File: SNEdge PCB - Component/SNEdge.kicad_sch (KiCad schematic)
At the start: 47 parts, among them J1 RGB_OUT, J2 (R-Y)O, J3 (B-Y)O, J4 YO, J5 G_IN, J6 B_IN, J7 R_IN, U2 TS5V330CPWR

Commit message: Cleaned up component side
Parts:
- removed R2: 1k, Resistor_SMD:R_0805_2012Metric_Pad1.20x1.40mm_HandSolder, symbol Device:R_US
- removed R3: 820R, Resistor_SMD:R_0805_2012Metric_Pad1.20x1.40mm_HandSolder, symbol Device:R_US
- removed R4: 220R, Resistor_SMD:R_0805_2012Metric_Pad1.20x1.40mm_HandSolder, symbol Device:R_US
- removed R5: 470R, Resistor_SMD:R_0805_2012Metric_Pad1.20x1.40mm_HandSolder, symbol Device:R_US
- removed R6: 680R, Resistor_SMD:R_0805_2012Metric_Pad1.20x1.40mm_HandSolder, symbol Device:R_US
- R1: value 1k -> 75
- R21: value 1k -> 10k
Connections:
- net GND: now also R1.1
- net at C2.1: now also J3.1 (In)
- net at J4.1 (In): now also C3.1
- net at J2.1 (In): now also C1.1, R1.2; no longer R1.1
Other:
- moved on the sheet: J2, J3, J4

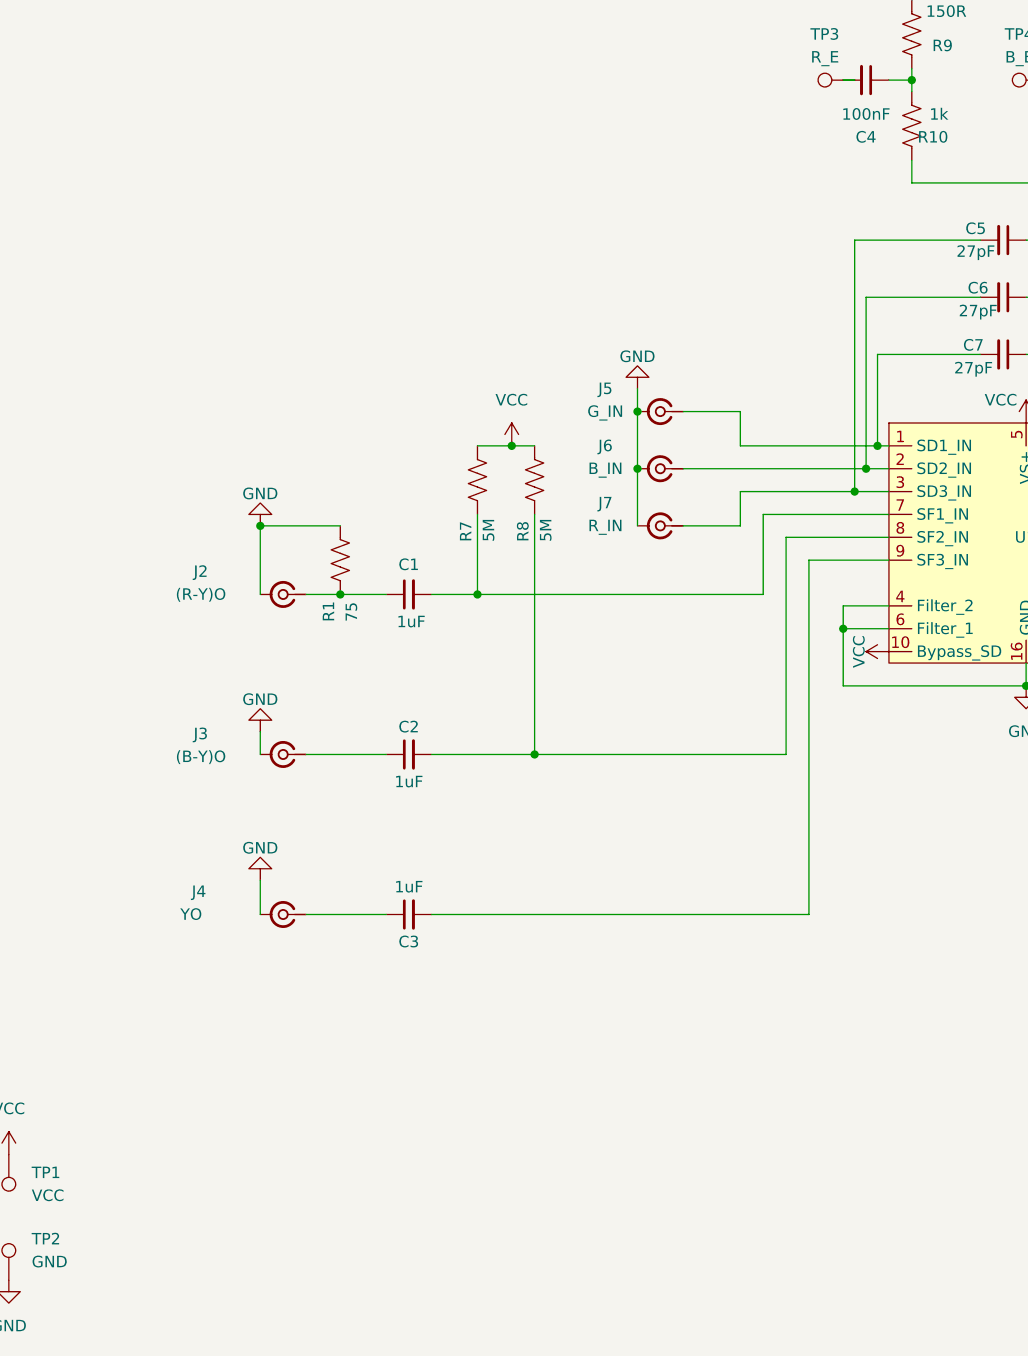
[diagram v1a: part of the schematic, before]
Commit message: Added voltage dividers on RGB input
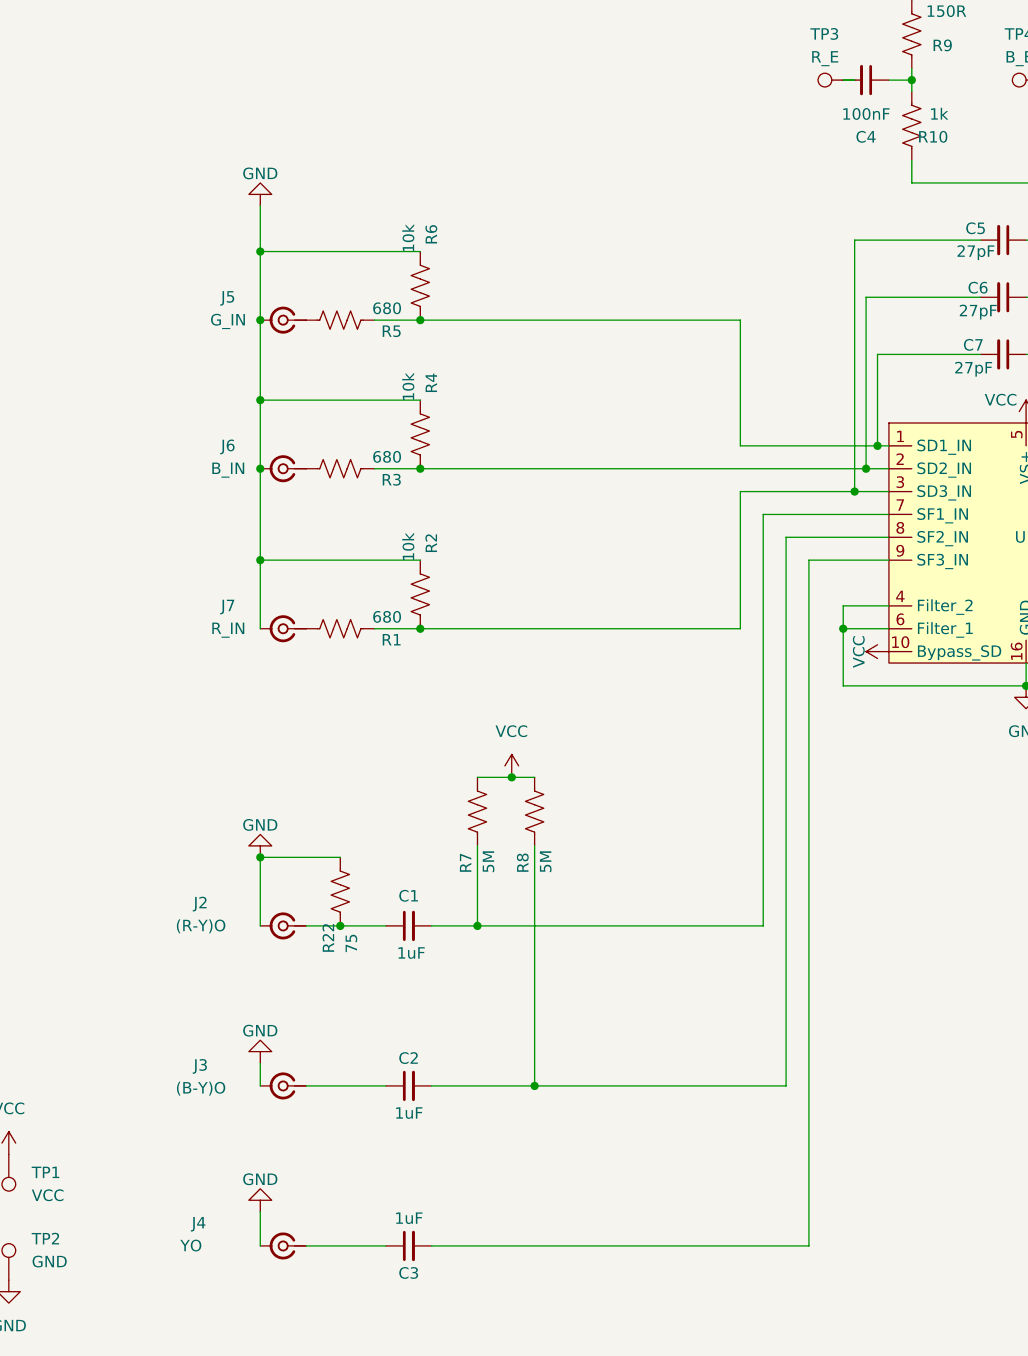
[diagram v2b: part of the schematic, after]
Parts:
- added R1, R3, R5: 680, Resistor_SMD:R_0805_2012Metric_Pad1.20x1.40mm_HandSolder, symbol Device:R_US
- added R2, R4, R6: 10k, Resistor_SMD:R_0805_2012Metric_Pad1.20x1.40mm_HandSolder, symbol Device:R_US
- renumbered R1 to R22
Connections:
- net GND: now also R2.2, R4.2, R6.2
- net at C7.2, U1.1 (SD1_IN): now also R5.2, R6.1; no longer J5.1 (In)
- net at C6.2, U1.2 (SD2_IN): now also R3.2, R4.1; no longer J6.1 (In)
- net at C5.2, U1.3 (SD3_IN): now also R1.2, R2.1; no longer J7.1 (In)
- new net: J6.1 (In), R3.1
- new net: J5.1 (In), R5.1
- new net: J7.1 (In), R1.1
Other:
- moved on the sheet: C1, C2, C3, J2, J3, J4, J5, J6, J7, R22, R7, R8

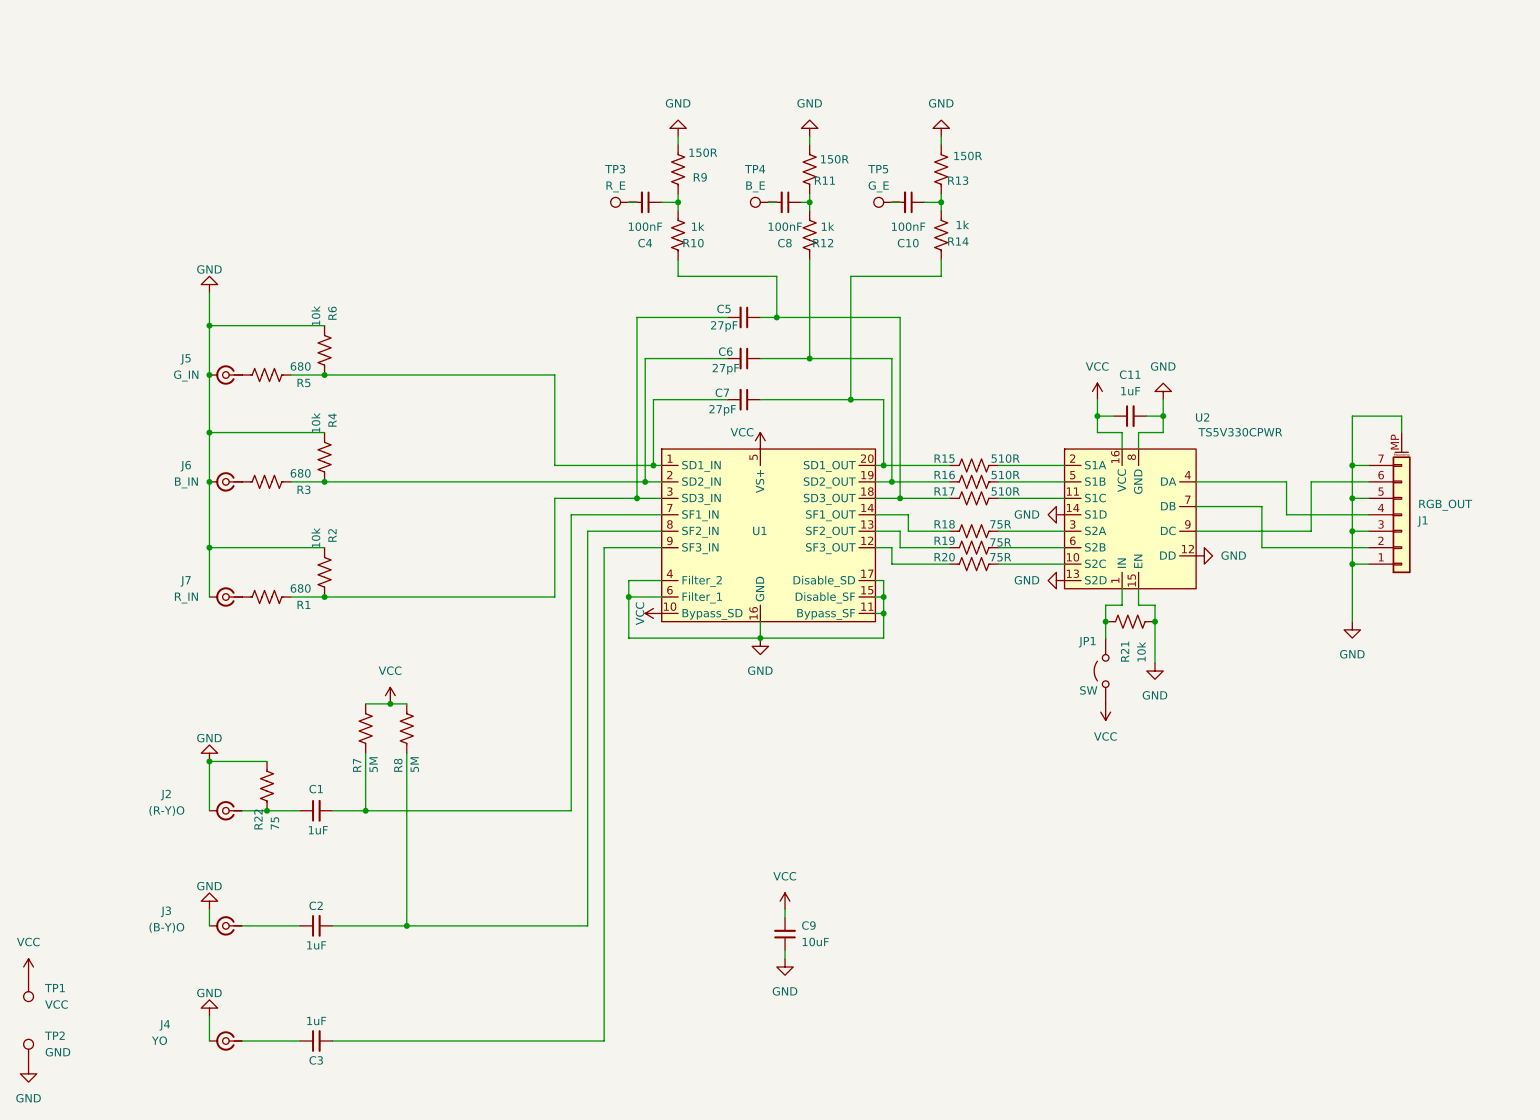
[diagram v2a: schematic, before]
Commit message: Remove component inputs and switch, refine SNEdge
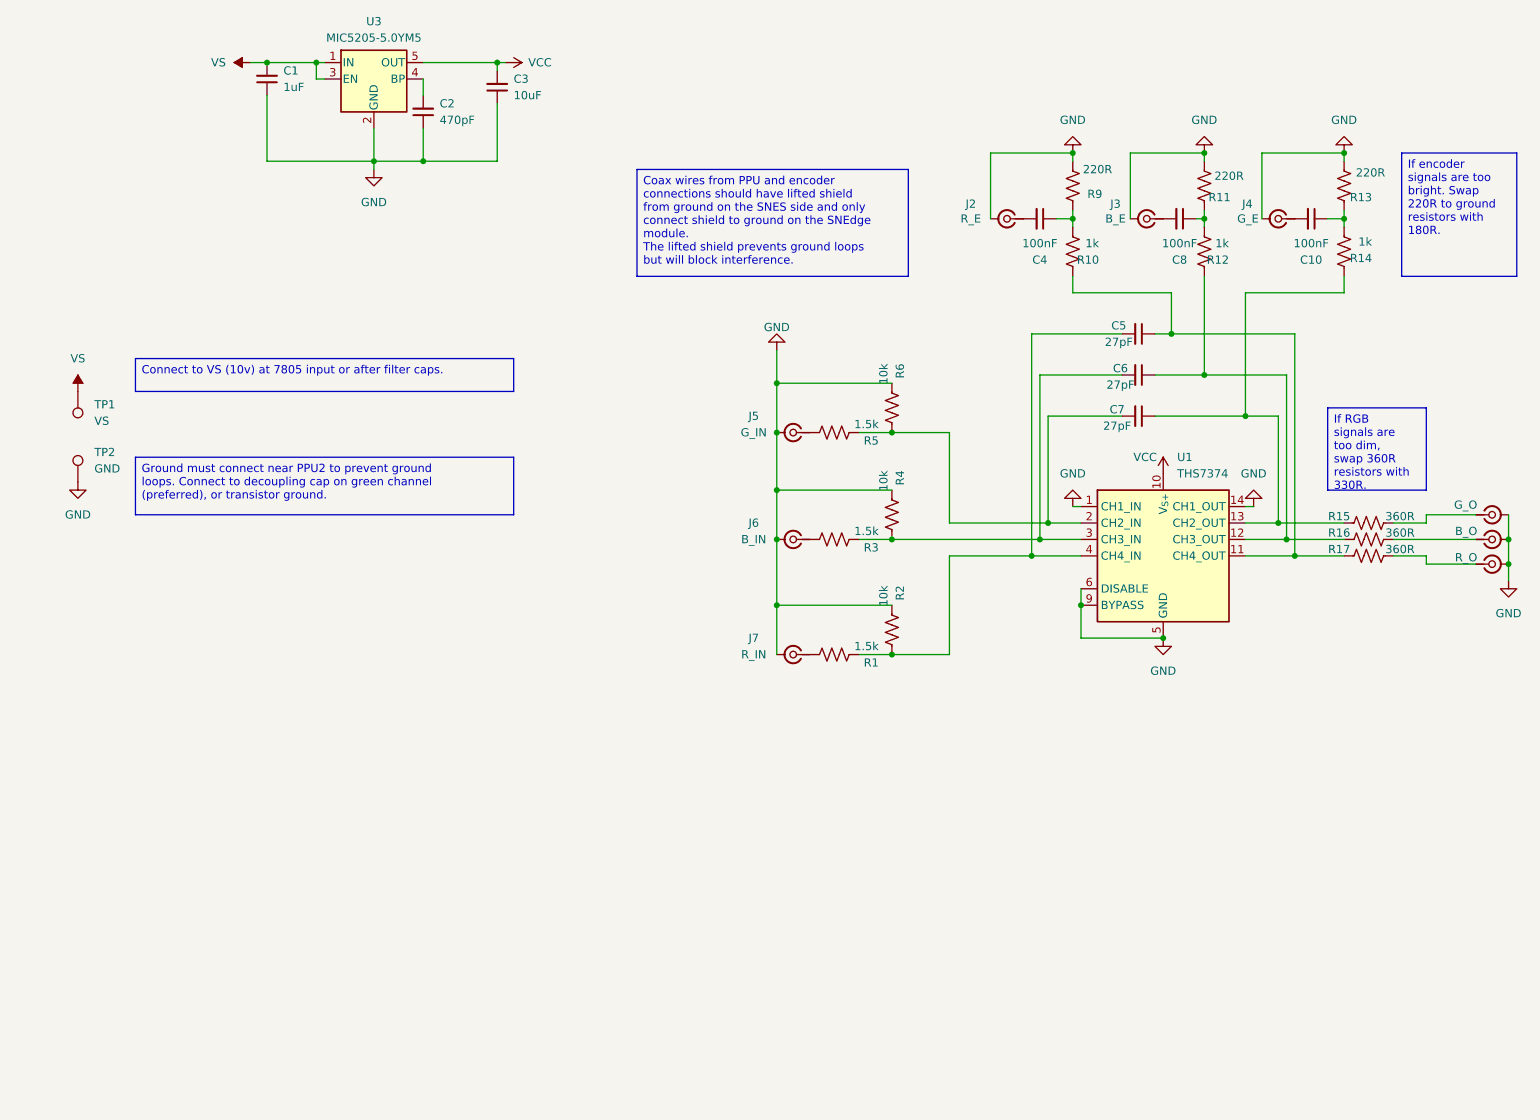
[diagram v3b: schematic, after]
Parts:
- removed C11: 1uF, Capacitor_SMD:C_0805_2012Metric_Pad1.18x1.45mm_HandSolder, symbol Device:C_Small
- removed C9: 10uF, Capacitor_SMD:C_0805_2012Metric_Pad1.18x1.45mm_HandSolder, symbol Device:C_Small
- removed J1: RGB_OUT, TT_Connectors:CON_527460771_MOL, symbol Connector_Generic_MountingPin:Conn_01x07_MountingPin
- removed JP1: SW, Jumper:SolderJumper-2_P1.3mm_Open_RoundedPad1.0x1.5mm, symbol Jumper:Jumper_2_Open
- removed R18, R19, R20: 75R, Resistor_SMD:R_0805_2012Metric_Pad1.20x1.40mm_HandSolder, symbol Device:R_US
- removed R21: 10k, Resistor_SMD:R_0805_2012Metric_Pad1.20x1.40mm_HandSolder, symbol Device:R_US
- removed R22: 75, Resistor_SMD:R_0805_2012Metric_Pad1.20x1.40mm_HandSolder, symbol Device:R_US
- removed R7, R8: 5M, Resistor_SMD:R_0805_2012Metric_Pad1.20x1.40mm_HandSolder, symbol Device:R_US
- removed TP3: R_E, TestPoint:TestPoint_Pad_1.5x1.5mm, symbol Connector:TestPoint
- removed TP4: B_E, TestPoint:TestPoint_Pad_1.5x1.5mm, symbol Connector:TestPoint
- removed TP5: G_E, TestPoint:TestPoint_Pad_1.5x1.5mm, symbol Connector:TestPoint
- removed U1: ~, Package_SO:TSSOP-20_4.4x6.5mm_P0.65mm, symbol SNEdge:THS7368
- removed U2: TS5V330CPWR, Package_SO:TSSOP-16_4.4x5mm_P0.65mm, symbol Project Symbols:TS5V330C
- added J10: R_O, Connector_Coaxial:U.FL_Hirose_U.FL-R-SMT-1_Vertical, symbol Connector:Conn_Coaxial_Small
- added J8: G_O, Connector_Coaxial:U.FL_Hirose_U.FL-R-SMT-1_Vertical, symbol Connector:Conn_Coaxial_Small
- added J9: B_O, Connector_Coaxial:U.FL_Hirose_U.FL-R-SMT-1_Vertical, symbol Connector:Conn_Coaxial_Small
- added U1: THS7374, Package_SO:TSSOP-14_4.4x5mm_P0.65mm, symbol Amplifier_Video:THS7374
- added U3: MIC5205-5.0YM5, Package_TO_SOT_SMD:SOT-23-5, symbol Regulator_Linear:MIC5205-5.0YM5
- C1, C10, C4, C8: Digi_PN 1276-2444-1-ND -> (none); MFG_PN CL21B104KBCNFNC -> (none)
- C2: value 1uF -> 470pF; Digi_PN 1276-2444-1-ND -> (none); MFG_PN CL21B104KBCNFNC -> (none)
- C3: value 1uF -> 10uF; Digi_PN 1276-2444-1-ND -> (none); MFG_PN CL21B104KBCNFNC -> (none)
- J2: value (R-Y)O -> R_E
- J3: value (B-Y)O -> B_E
- J4: value YO -> G_E
- R1, R3, R5: value 680 -> 1.5k
- R10, R12, R14: Digi_PN RMCF0805FT1K00CT-ND -> (none); MFG_PN RMCF0805FT1K00 -> (none)
- R11, R13, R9: value 150R -> 220R; Digi_PN RMCF0805FT150RCT-ND -> (none); MFG_PN RMCF0805FT150R -> (none)
- R15, R16, R17: value 510R -> 360R; Digi_PN RMCF0805FT510RCT-ND -> (none); MFG_PN RMCF0805FT510R -> (none)
- TP1: value VCC -> VS
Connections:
- net GND: now also C1.1, C2.1, C3.1, J10.2 (Ext), J8.2 (Ext), J9.2 (Ext), U1.1 (CH1_IN), U1.14 (CH1_OUT), U1.5 (GND), U1.6 (DISABLE), U1.9 (BYPASS), U3.2 (GND)
- net VCC: now also C3.2, U1.10 (V_{S+}), U3.5 (OUT); no longer TP1.1
- net at C7.2, R5.2, R6.1: now also U1.2 (CH2_IN)
- net at C2.2: now also U3.4 (BP)
- net at C4.2: now also J2.1 (In)
- net at C5.1, R10.1, R17.2: now also U1.11 (CH4_OUT)
- net at C6.1, R12.1, R16.2: now also U1.12 (CH3_OUT)
- net at C6.2, R3.2, R4.1: now also U1.3 (CH3_IN)
- net at C7.1, R14.1, R15.2: now also U1.13 (CH2_OUT)
- net at C5.2, R1.2, R2.1: now also U1.4 (CH4_IN)
- net VS: now reaches C1.2
- net VS: now also TP1.1, U3.1 (IN), U3.3 (EN)
- net at R17.1: now also J10.1 (In)
- net at R16.1: now also J9.1 (In)
- net at R15.1: now also J8.1 (In)
- net at J3.1 (In): now also C8.2; no longer C2.1
- net at J4.1 (In): now also C10.2; no longer C3.1
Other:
- company: Thunder Technologies -> Innov8bit
- moved on the sheet: C10, C4, C5, C6, C7, C8, J2, J3, J4, J5, J6, J7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
